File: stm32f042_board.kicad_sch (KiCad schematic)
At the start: 24 parts, among them J1 Conn_01x12_Female, J2 Conn_01x12_Female, J3 USB_B_Micro, J5 JTAG/SWD, U1 STM32F042F6Px, U2 MCP1802, U3 USBLC6-2SC6

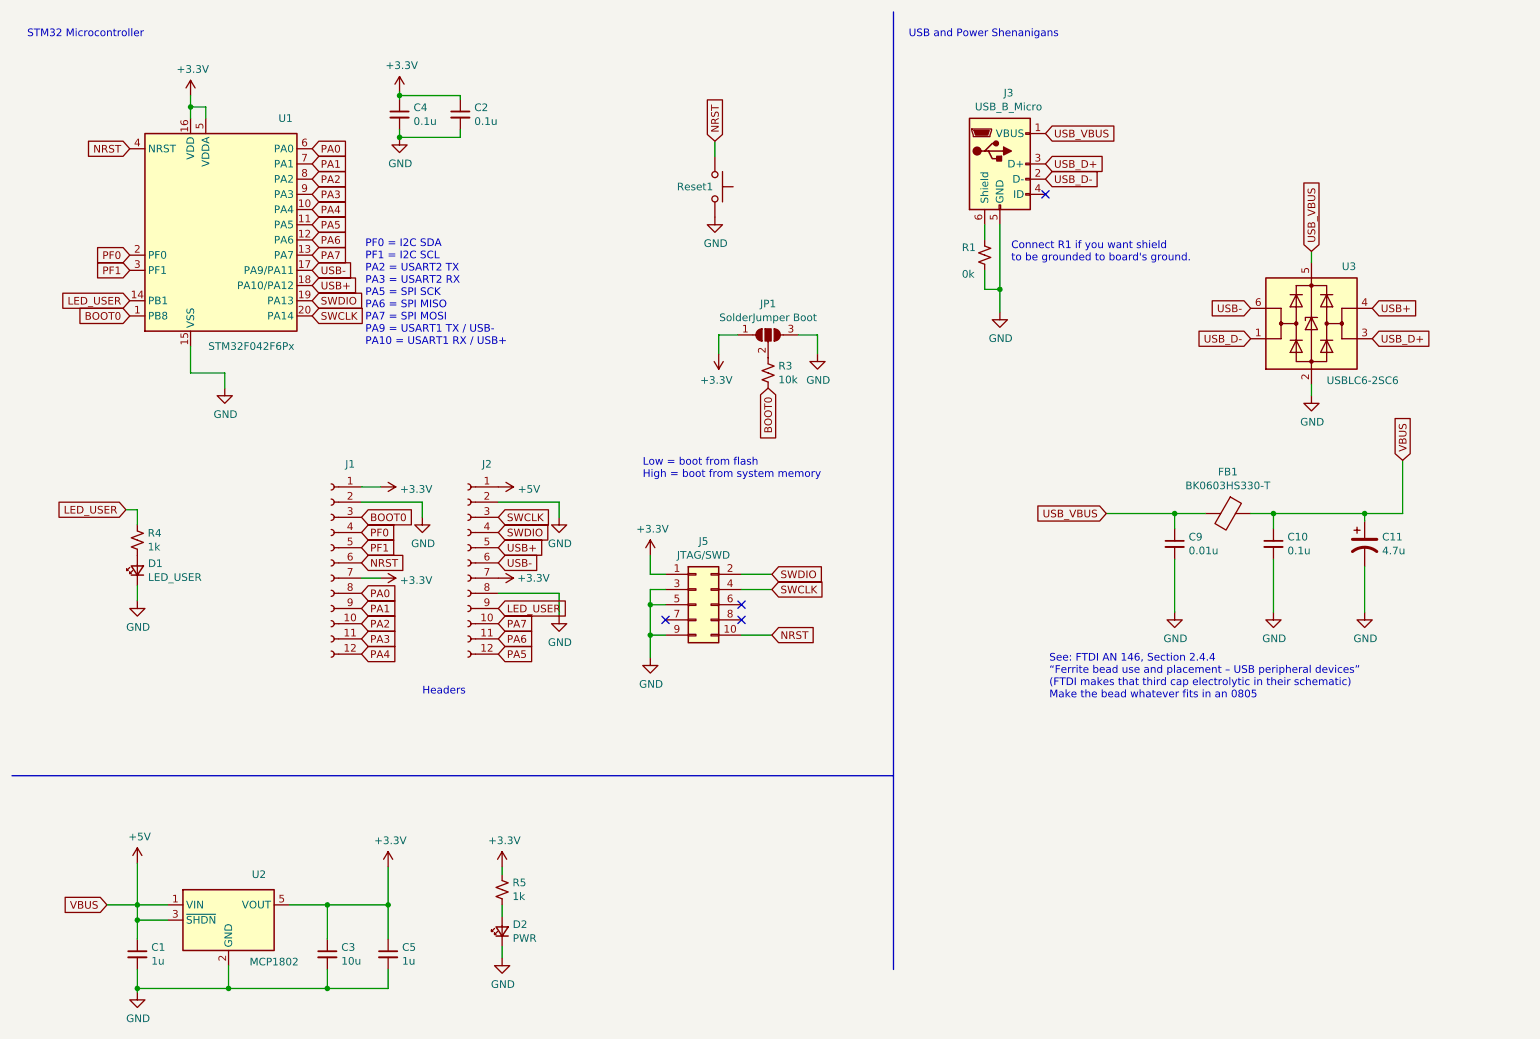
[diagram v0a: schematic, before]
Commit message: Replace USB Micro receptacle with USB C
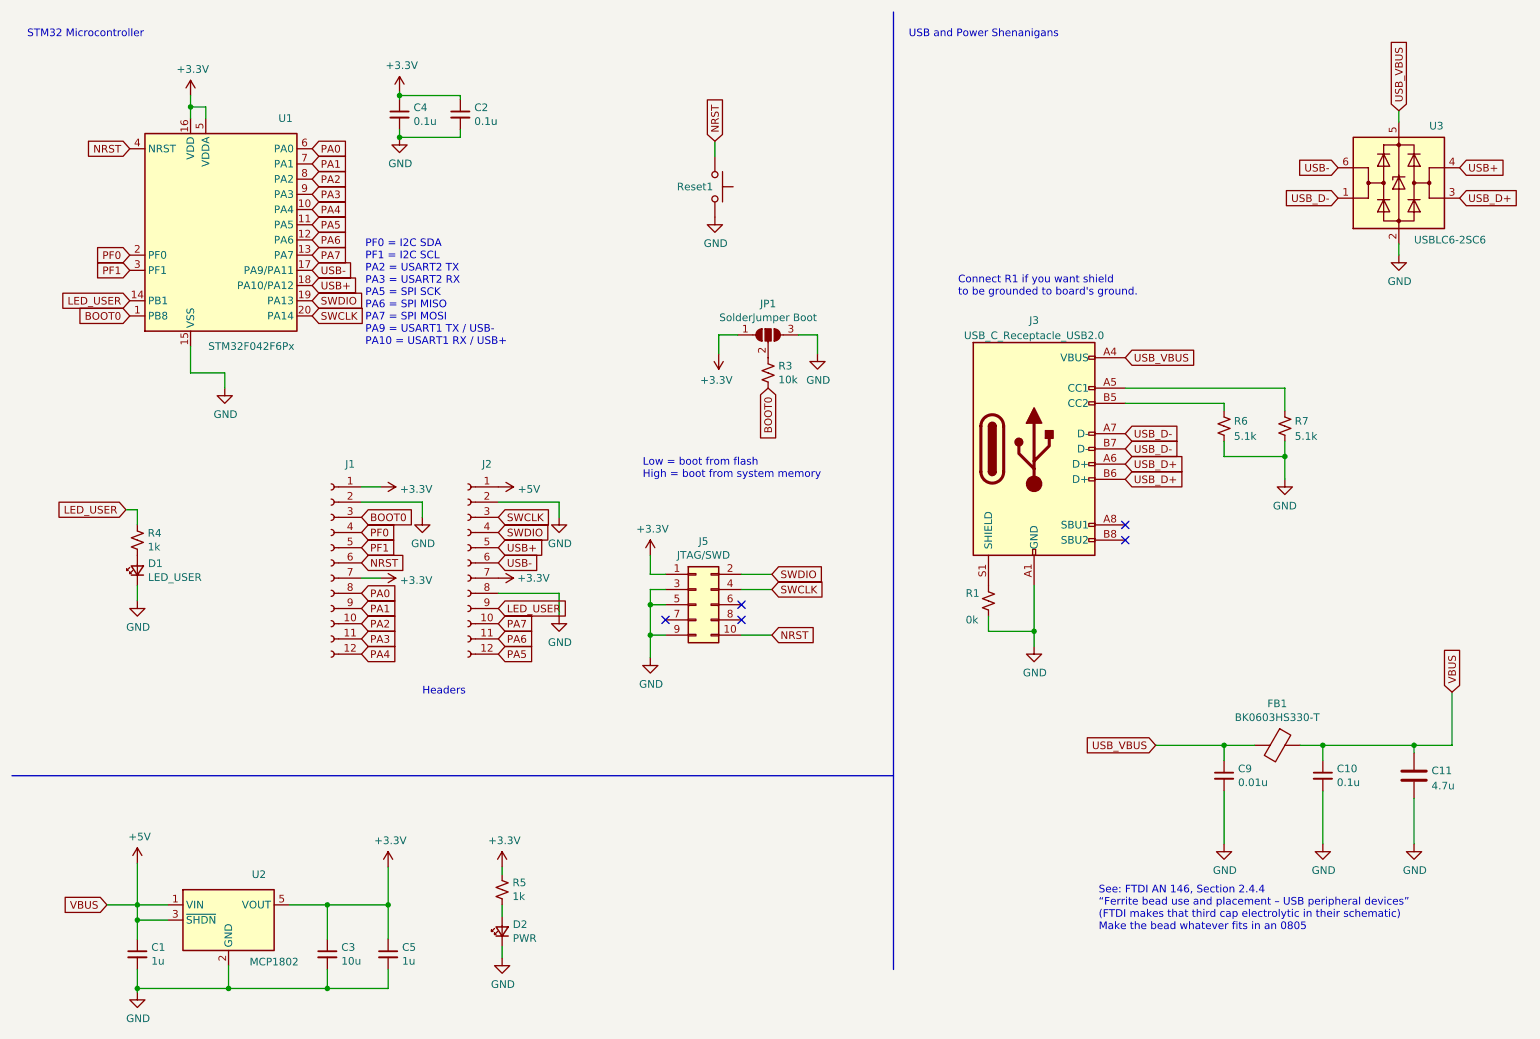
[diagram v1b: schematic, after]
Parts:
- removed C11: 4.7u, Capacitor_SMD:CP_Elec_4x4.5, symbol stm32f042_board-rescue:CP1-Device
- removed J3: USB_B_Micro, Connector_USB:USB_Micro-B_Molex-105017-0001, symbol Connector:USB_B_Micro
- added C11: 4.7u, Capacitor_SMD:C_1206_3216Metric, symbol Device:C
- added J3: USB_C_Receptacle_USB2.0, USBC_Receptacle:USB4105-GF-A, symbol Connector:USB_C_Receptacle_USB2.0
- added R6, R7: 5.1k, Resistor_SMD:R_0603_1608Metric, symbol Device:R_Small_US
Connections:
- net +5V: now also C11.1
- net GND: now also C11.2, J3.A1 (GND), J3.A12 (GND), J3.B1 (GND), J3.B12 (GND), R6.2, R7.2
- net USB_D+: now also J3.A6 (D+), J3.B6 (D+)
- net USB_D-: now also J3.A7 (D-), J3.B7 (D-)
- net USB_VBUS: now also J3.A4 (VBUS), J3.A9 (VBUS), J3.B4 (VBUS), J3.B9 (VBUS)
- net at R1.1: now also J3.S1 (SHIELD)
- new net: J3.A5 (CC1), R7.1
- new net: J3.B5 (CC2), R6.1
- no-connect marks 4 -> 5
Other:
- moved on the sheet: C10, C9, FB1, R1, U3
